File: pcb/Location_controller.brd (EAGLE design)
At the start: 100 x 80 mm, 1 part

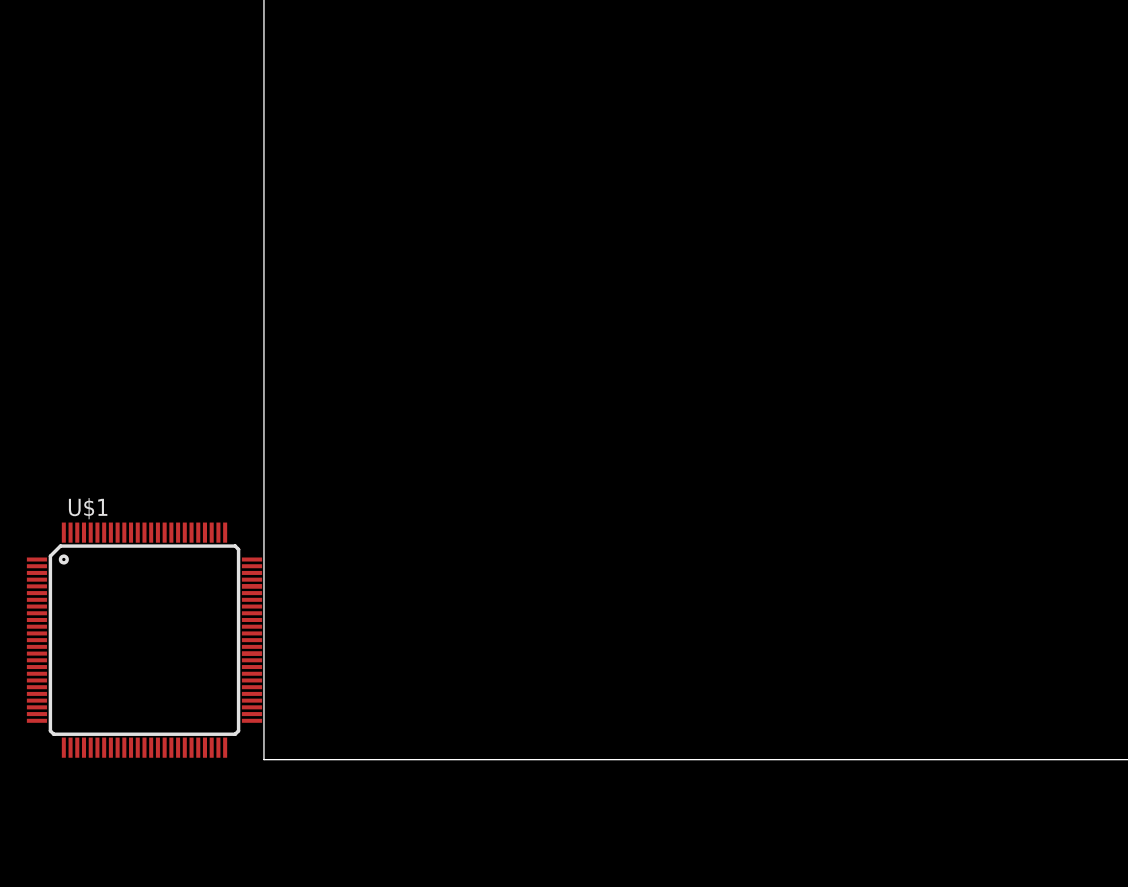
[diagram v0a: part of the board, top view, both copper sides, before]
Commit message: Add crystal to layout
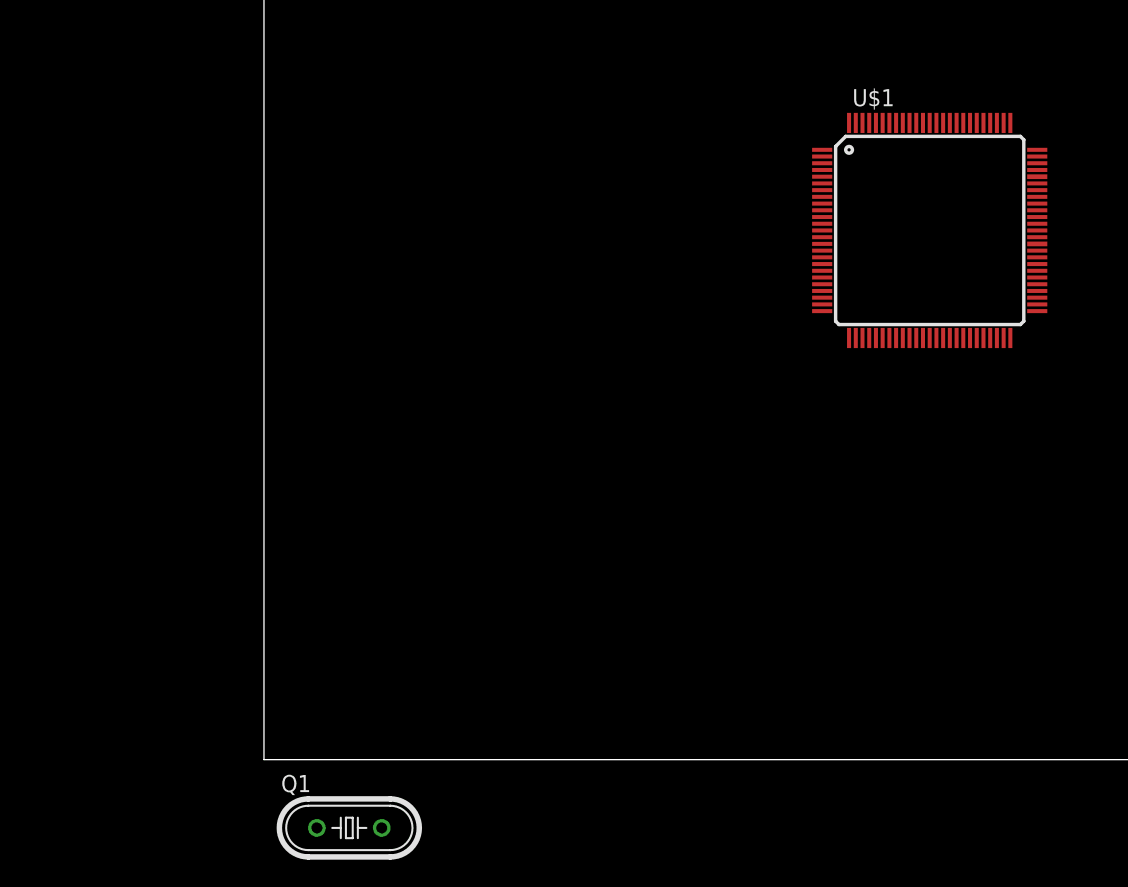
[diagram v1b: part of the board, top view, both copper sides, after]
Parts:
- added Q1: (no value), crystal:HC49/S
- moved U$1 65.9 mm to (49.5, 39.4)
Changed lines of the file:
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@@
 </autorouter>
 <elements>
-<element name="U$1" library="stm32f4" package="TQFP100" value="STM32F407V" x="-8.89" y="8.89"/>
+<element name="U$1" library="stm32f4" package="TQFP100" value="STM32F407V" x="49.53" y="39.37"/>
+<element name="Q1" library="crystal" package="HC49/S" value="" x="6.35" y="-5.08">
+<attribute name="OC_NEWARK" value="unknown" x="6.35" y="-5.08" size="1.778" layer="27" display="off"/>
+<attribute name="MPN" value="" x="6.35" y="-5.08" size="1.778" layer="27" display="off"/>
+<attribute name="MF" value="" x="6.35" y="-5.08" size="1.778" layer="27" display="off"/>
+<attribute name="OC_FARNELL" value="1667008" x="6.35" y="-5.08" size="1.778" layer="27" display="off"/>
+</element>
 </elements>
 <signals>

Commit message: Add Crystal to Layout
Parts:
- added C1, C2: 20p, eagle-ltspice:C0805
- added R1: 0, eagle-ltspice:R0805
- added R2: 220, eagle-ltspice:R0805
- moved Q1 48.7 mm to (19.1, 41.9), turned to 90 degrees
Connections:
- new net GND: C1.2, C2.2
- new net N$1: C2.1, Q1.1, R2.1
- new net N$2: C1.1, Q1.2, R1.1
- new net OSC_IN: R1.2, U$1.12
- new net OSC_OUT: R2.2, U$1.13
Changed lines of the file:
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@@
 <layer number="97" name="Info" color="7" fill="1" visible="no" active="no"/>
 <layer number="98" name="Guide" color="6" fill="1" visible="no" active="no"/>
+<layer number="99" name="SpiceOrder" color="5" fill="1" visible="no" active="no"/>
 <layer number="100" name="Muster" color="7" fill="1" visible="no" active="no"/>
 <layer number="101" name="Patch_Top" color="12" fill="4" visible="yes" active="yes"/>
@@
 <elements>
 <element name="U$1" library="stm32f4" package="TQFP100" value="STM32F407V" x="49.53" y="39.37"/>
-<element name="Q1" library="crystal" package="HC49/S" value="" x="6.35" y="-5.08">
-<attribute name="OC_NEWARK" value="unknown" x="6.35" y="-5.08" size="1.778" layer="27" display="off"/>
-<attribute name="MPN" value="" x="6.35" y="-5.08" size="1.778" layer="27" display="off"/>
-<attribute name="MF" value="" x="6.35" y="-5.08" size="1.778" layer="27" display="off"/>
-<attribute name="OC_FARNELL" value="1667008" x="6.35" y="-5.08" size="1.778" layer="27" display="off"/>
+<element name="Q1" library="crystal" package="HC49/S" value="" x="19.05" y="41.91" rot="R90">
+<attribute name="OC_NEWARK" value="unknown" x="19.05" y="41.91" size="1.778" layer="27" rot="R90" display="off"/>
+<attribute name="MPN" value="" x="19.05" y="41.91" size="1.778" layer="27" rot="R90" display="off"/>
+<attribute name="MF" value="" x="19.05" y="41.91" size="1.778" layer="27" rot="R90" display="off"/>
+<attribute name="OC_FARNELL" value="1667008" x="19.05" y="41.91" size="1.778" layer="27" rot="R90" display="off"/>
+</element>
+<element name="C1" library="eagle-ltspice" package="C0805" value="20p" x="7.62" y="44.45" rot="R180">
+<attribute name="SPICEMODEL" value="NONE" x="7.62" y="44.45" size="1.778" layer="27" rot="R180" display="off"/>
+<attribute name="SPICEPREFIX" value="C" x="7.62" y="44.45" size="1.778" layer="27" rot="R180" display="off"/>
+</element>
+<element name="C2" library="eagle-ltspice" package="C0805" value="20p" x="7.62" y="39.37" rot="R180">
+<attribute name="SPICEMODEL" value="NONE" x="7.62" y="39.37" size="1.778" layer="27" rot="R180" display="off"/>
+<attribute name="SPICEPREFIX" value="C" x="7.62" y="39.37" size="1.778" layer="27" rot="R180" display="off"/>
+</element>
+<element name="R1" library="eagle-ltspice" package="R0805" value="0" x="31.75" y="44.45" rot="R180">
+<attribute name="SPICEMODEL" value="NONE" x="31.75" y="44.45" size="1.778" layer="27" rot="R180" display="off"/>
+<attribute name="SPICEPREFIX" value="R" x="31.75" y="44.45" size="1.778" layer="27" rot="R180" display="off"/>
+</element>
+<element name="R2" library="eagle-ltspice" package="R0805" value="220" x="31.75" y="38.1">
+<attribute name="SPICEMODEL" value="NONE" x="31.75" y="38.1" size="1.778" layer="27" display="off"/>
+<attribute name="SPICEPREFIX" value="R" x="31.75" y="38.1" size="1.778" layer="27" display="off"/>
 </element>
 </elements>
 <signals>
+<signal name="OSC_IN">
+<contactref element="U$1" pad="12"/>
+<contactref element="R1" pad="2"/>
+<wire x1="30.8" y1="44.45" x2="41.53" y2="39.87" width="0" layer="19" extent="1-1"/>
+</signal>
+<signal name="OSC_OUT">
+<contactref element="U$1" pad="13"/>
+<contactref element="R2" pad="2"/>
+<wire x1="32.7" y1="38.1" x2="41.53" y2="39.37" width="0" layer="19" extent="1-1"/>
+</signal>
+<signal name="GND">
+<contactref element="C2" pad="2"/>
+<contactref element="C1" pad="2"/>
+<wire x1="6.67" y1="39.37" x2="6.67" y2="44.45" width="0" layer="19" extent="1-1"/>
+</signal>
+<signal name="N$1">
+<contactref element="Q1" pad="1"/>
+<contactref element="C2" pad="1"/>
+<contactref element="R2" pad="1"/>
+<wire x1="19.05" y1="39.497" x2="30.8" y2="38.1" width="0" layer="19" extent="1-1"/>
+<wire x1="8.57" y1="39.37" x2="19.05" y2="39.497" width="0" layer="19" extent="1-1"/>
+</signal>
+<signal name="N$2">
+<contactref element="Q1" pad="2"/>
+<contactref element="C1" pad="1"/>
+<contactref element="R1" pad="1"/>
+<wire x1="19.05" y1="44.323" x2="32.7" y2="44.45" width="0" layer="19" extent="1-1"/>
+<wire x1="8.57" y1="44.45" x2="19.05" y2="44.323" width="0" layer="19" extent="1-1"/>
+</signal>
 </signals>
 </board>

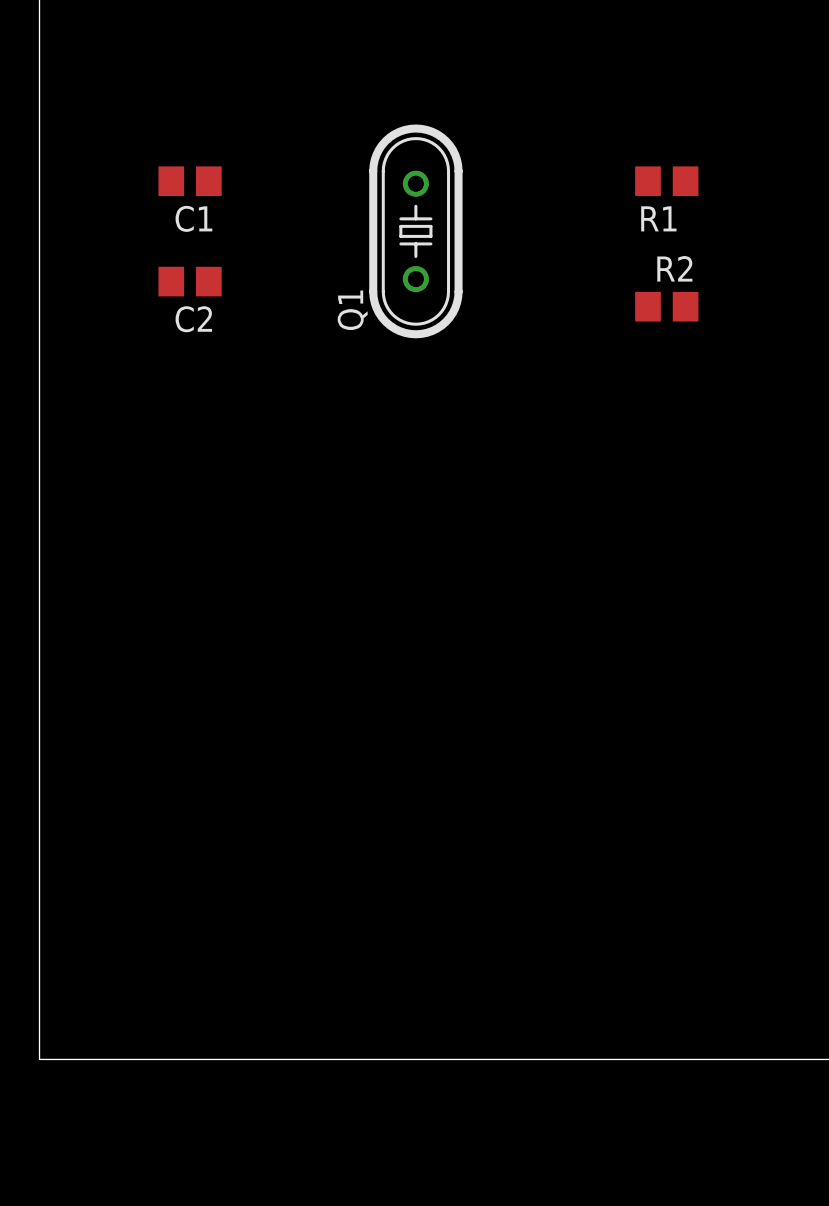
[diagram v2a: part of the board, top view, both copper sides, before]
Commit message: Add Accelerometer to PCB
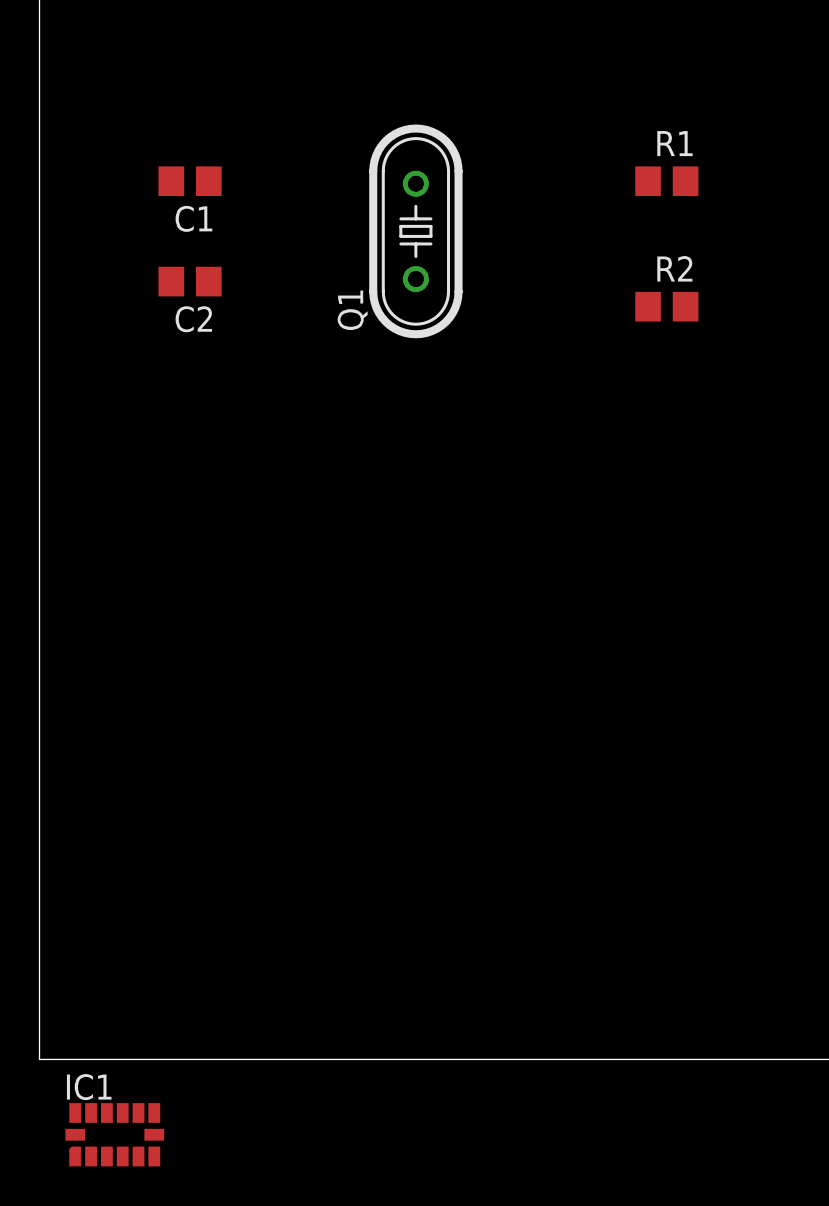
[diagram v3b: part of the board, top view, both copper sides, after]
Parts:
- added IC1: LIS302DL, stm32f4:LGA-14
- turned R1 to 0 degrees
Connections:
- new net VDD: IC1.6
- new net VDD_IO: IC1.1
- net GND: now also IC1.2
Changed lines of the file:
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@@
 <attribute name="SPICEPREFIX" value="C" x="7.62" y="39.37" size="1.778" layer="27" rot="R180" display="off"/>
 </element>
-<element name="R1" library="eagle-ltspice" package="R0805" value="0" x="31.75" y="44.45" rot="R180">
-<attribute name="SPICEMODEL" value="NONE" x="31.75" y="44.45" size="1.778" layer="27" rot="R180" display="off"/>
-<attribute name="SPICEPREFIX" value="R" x="31.75" y="44.45" size="1.778" layer="27" rot="R180" display="off"/>
+<element name="R1" library="eagle-ltspice" package="R0805" value="0" x="31.75" y="44.45">
+<attribute name="SPICEMODEL" value="NONE" x="31.75" y="44.45" size="1.778" layer="27" display="off"/>
+<attribute name="SPICEPREFIX" value="R" x="31.75" y="44.45" size="1.778" layer="27" display="off"/>
 </element>
 <element name="R2" library="eagle-ltspice" package="R0805" value="220" x="31.75" y="38.1">
@@
 <attribute name="SPICEPREFIX" value="R" x="31.75" y="38.1" size="1.778" layer="27" display="off"/>
 </element>
+<element name="IC1" library="stm32f4" package="LGA-14" value="LIS302DL" x="3.81" y="-3.81"/>
 </elements>
 <signals>
@@
 <contactref element="U$1" pad="12"/>
 <contactref element="R1" pad="2"/>
-<wire x1="30.8" y1="44.45" x2="41.53" y2="39.87" width="0" layer="19" extent="1-1"/>
+<wire x1="32.7" y1="44.45" x2="41.53" y2="39.87" width="0" layer="19" extent="1-1"/>
 </signal>
 <signal name="OSC_OUT">
@@
 <contactref element="C2" pad="2"/>
 <contactref element="C1" pad="2"/>
+<contactref element="IC1" pad="2"/>
 <wire x1="6.67" y1="39.37" x2="6.67" y2="44.45" width="0" layer="19" extent="1-1"/>
+<wire x1="2.61" y1="-4.91" x2="6.67" y2="39.37" width="0" layer="19" extent="1-1"/>
 </signal>
 <signal name="N$1">
@@
 <contactref element="C1" pad="1"/>
 <contactref element="R1" pad="1"/>
-<wire x1="19.05" y1="44.323" x2="32.7" y2="44.45" width="0" layer="19" extent="1-1"/>
+<wire x1="19.05" y1="44.323" x2="30.8" y2="44.45" width="0" layer="19" extent="1-1"/>
 <wire x1="8.57" y1="44.45" x2="19.05" y2="44.323" width="0" layer="19" extent="1-1"/>
 </signal>
+<signal name="VDD_IO">
+<contactref element="IC1" pad="1"/>
+</signal>
+<signal name="VDD">
+<contactref element="IC1" pad="6"/>
+</signal>
 </signals>

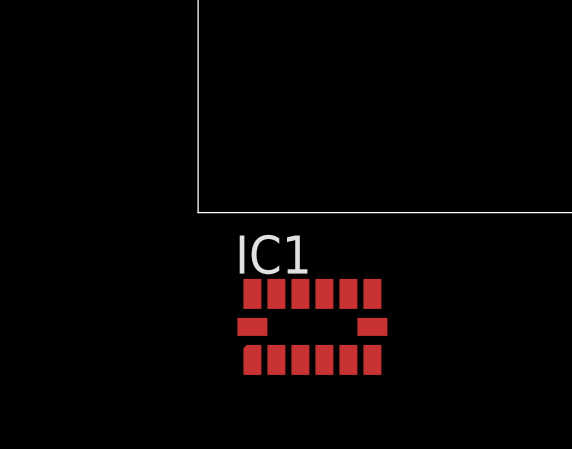
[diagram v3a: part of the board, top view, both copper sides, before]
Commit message: Add Gyroscope to PCB
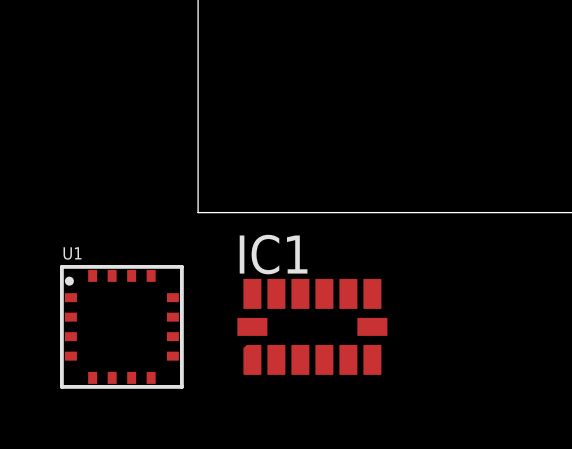
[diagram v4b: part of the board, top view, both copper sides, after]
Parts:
- added U1: L3G4200DH, stm32f4:LGA-16L
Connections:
- new net RES(GND): U1.10, U1.11, U1.12, U1.8, U1.9
- new net RES(VDD): U1.15
- net GND: now also U1.13
- net VDD: now also U1.16
- net VDD_IO: now also U1.1
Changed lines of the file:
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@@
 <layer number="101" name="Patch_Top" color="12" fill="4" visible="yes" active="yes"/>
 <layer number="102" name="Vscore" color="7" fill="1" visible="yes" active="yes"/>
+<layer number="103" name="tMap" color="7" fill="1" visible="yes" active="yes"/>
 <layer number="104" name="Name" color="7" fill="1" visible="yes" active="yes"/>
+<layer number="105" name="tPlate" color="7" fill="1" visible="yes" active="yes"/>
+<layer number="106" name="bPlate" color="7" fill="1" visible="yes" active="yes"/>
+<layer number="107" name="Crop" color="7" fill="1" visible="yes" active="yes"/>
 <layer number="116" name="Patch_BOT" color="9" fill="4" visible="yes" active="yes"/>
 <layer number="121" name="_tsilk" color="7" fill="1" visible="yes" active="yes"/>
@@
 <layer number="201" name="201bmp" color="2" fill="1" visible="no" active="no"/>
 <layer number="202" name="202bmp" color="3" fill="1" visible="no" active="no"/>
+<layer number="203" name="203bmp" color="4" fill="10" visible="yes" active="yes"/>
+<layer number="204" name="204bmp" color="5" fill="10" visible="yes" active="yes"/>
+<layer number="205" name="205bmp" color="6" fill="10" visible="yes" active="yes"/>
+<layer number="206" name="206bmp" color="7" fill="10" visible="yes" active="yes"/>
+<layer number="207" name="207bmp" color="8" fill="10" visible="yes" active="yes"/>
+<layer number="208" name="208bmp" color="9" fill="10" visible="yes" active="yes"/>
 <layer number="250" name="Descript" color="3" fill="1" visible="no" active="no"/>
 <layer number="251" name="SMDround" color="12" fill="11" visible="no" active="no"/>
@@
 </element>
 <element name="IC1" library="stm32f4" package="LGA-14" value="LIS302DL" x="3.81" y="-3.81"/>
+<element name="U1" library="stm32f4" package="LGA-16L" value="L3G4200DH" x="-2.54" y="-3.81"/>
 </elements>
 <signals>
@@
 <contactref element="C1" pad="2"/>
 <contactref element="IC1" pad="2"/>
+<contactref element="U1" pad="13"/>
 <wire x1="6.67" y1="39.37" x2="6.67" y2="44.45" width="0" layer="19" extent="1-1"/>
-<wire x1="2.61" y1="-4.91" x2="6.67" y2="39.37" width="0" layer="19" extent="1-1"/>
+<wire x1="-1.565" y1="-2.11" x2="6.67" y2="39.37" width="0" layer="19" extent="1-1"/>
+<wire x1="2.61" y1="-4.91" x2="-1.565" y2="-2.11" width="0" layer="19" extent="1-1"/>
 </signal>
 <signal name="N$1">
@@
 <signal name="VDD_IO">
 <contactref element="IC1" pad="1"/>
+<contactref element="U1" pad="1"/>
+<wire x1="1.81" y1="-4.91" x2="-4.24" y2="-2.835" width="0" layer="19" extent="1-1"/>
 </signal>
 <signal name="VDD">
 <contactref element="IC1" pad="6"/>
+<contactref element="U1" pad="16"/>
+<wire x1="-3.515" y1="-2.11" x2="5.81" y2="-4.91" width="0" layer="19" extent="1-1"/>
+</signal>
+<signal name="RES(GND)">
+<contactref element="U1" pad="10"/>
+<contactref element="U1" pad="8"/>
+<contactref element="U1" pad="12"/>
+<contactref element="U1" pad="11"/>
+<contactref element="U1" pad="9"/>
+<wire x1="-0.84" y1="-4.785" x2="-1.565" y2="-5.51" width="0" layer="19" extent="1-1"/>
+<wire x1="-0.84" y1="-4.135" x2="-0.84" y2="-4.785" width="0" layer="19" extent="1-1"/>
+<wire x1="-0.84" y1="-3.485" x2="-0.84" y2="-4.135" width="0" layer="19" extent="1-1"/>
+<wire x1="-0.84" y1="-2.835" x2="-0.84" y2="-3.485" width="0" layer="19" extent="1-1"/>
+</signal>
+<signal name="RES(VDD)">
+<contactref element="U1" pad="15"/>
 </signal>
 </signals>
